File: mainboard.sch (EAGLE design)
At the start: 19 parts, among them J1 RASPBERRYPI-40-PIN-GPIO

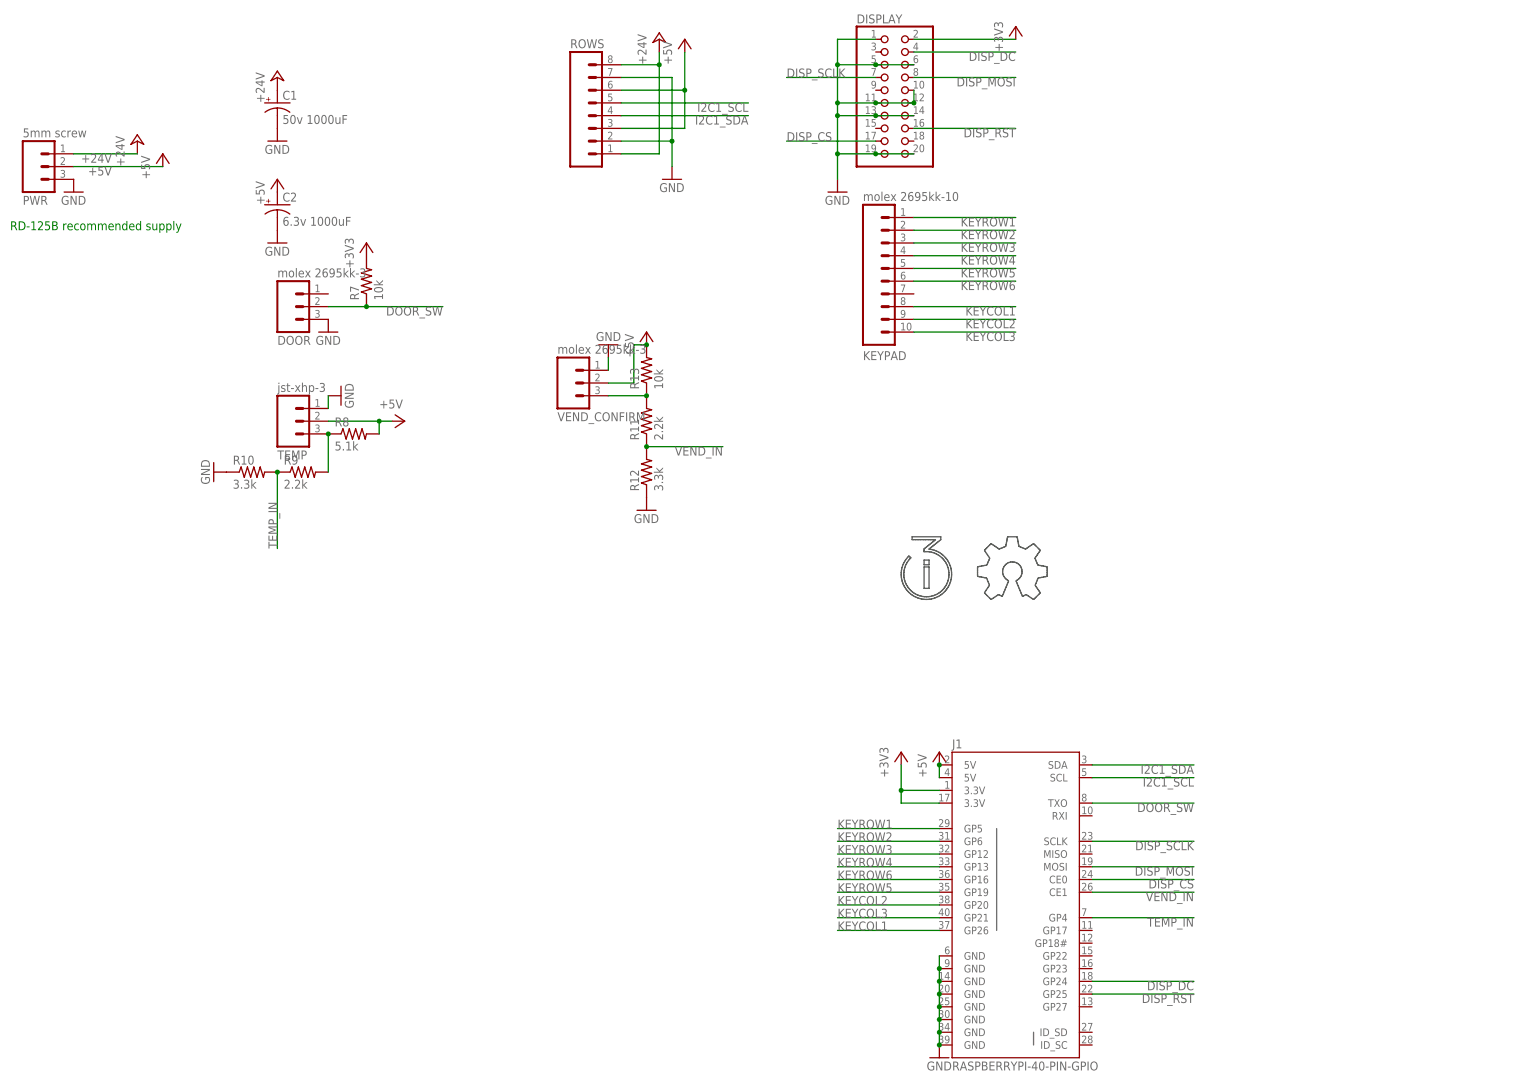
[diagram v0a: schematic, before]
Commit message: Completed mainboard design edits; buffers for keypad, reworked 5V feed.
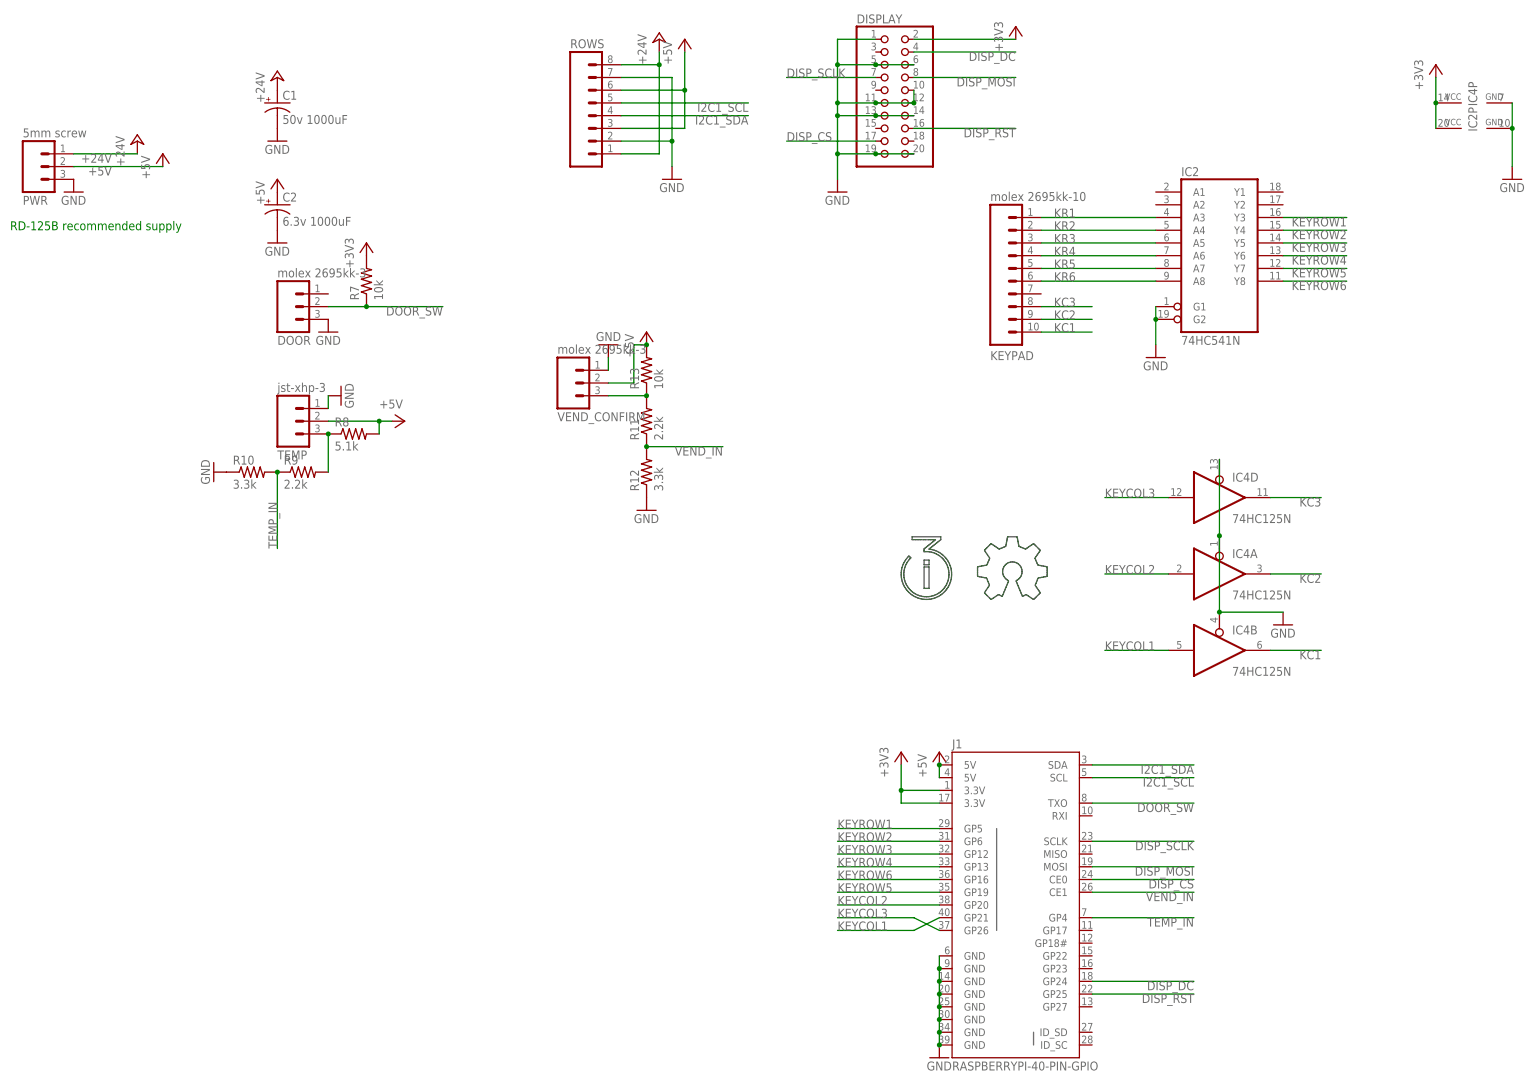
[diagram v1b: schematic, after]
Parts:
- added IC2: 74HC541N, 74xx-eu:74HC541N
- added IC4: 74HC125N, 74xx-eu:74HC125N
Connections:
- new net KC1: IC4B.O, KEYPAD.10
- new net KC2: IC4A.O, KEYPAD.9
- new net KC3: IC4D.O, KEYPAD.8
- new net KR1: IC2A.A3, KEYPAD.1
- new net KR2: IC2A.A4, KEYPAD.2
- new net KR3: IC2A.A5, KEYPAD.3
- new net KR4: IC2A.A6, KEYPAD.4
- new net KR5: IC2A.A7, KEYPAD.5
- new net KR6: IC2A.A8, KEYPAD.6
- net +3V3: now also IC2P.VCC, IC4P.VCC
- net GND: now also IC2A.G1, IC2A.G2, IC2P.GND, IC4A.OE, IC4B.OE, IC4D.OE, IC4P.GND
- net KEYCOL1: now also IC4B.I, J1.GP21; no longer J1.GP26, KEYPAD.8
- net KEYCOL2: now also IC4A.I; no longer KEYPAD.9
- net KEYCOL3: now also IC4D.I, J1.GP26; no longer J1.GP21, KEYPAD.10
- net KEYROW1: now also IC2A.Y3; no longer KEYPAD.1
- net KEYROW2: now also IC2A.Y4; no longer KEYPAD.2
- net KEYROW3: now also IC2A.Y5; no longer KEYPAD.3
- net KEYROW4: now also IC2A.Y6; no longer KEYPAD.4
- net KEYROW5: now also IC2A.Y7; no longer KEYPAD.5
- net KEYROW6: now also IC2A.Y8; no longer KEYPAD.6
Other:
- moved on the sheet: KEYPAD

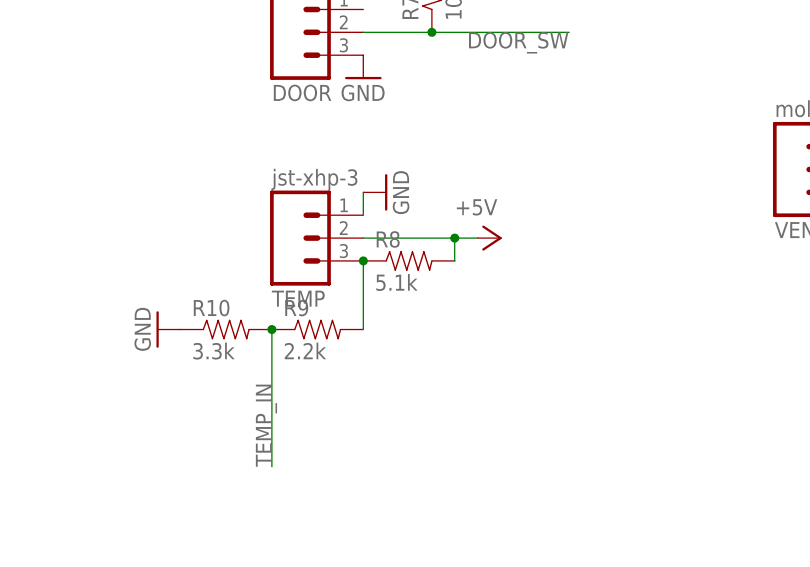
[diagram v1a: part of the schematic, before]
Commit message: No the one-wire sensor does not need a $0.252 resistor as a pull-up the $0.0254 ones are fine kthxbai.
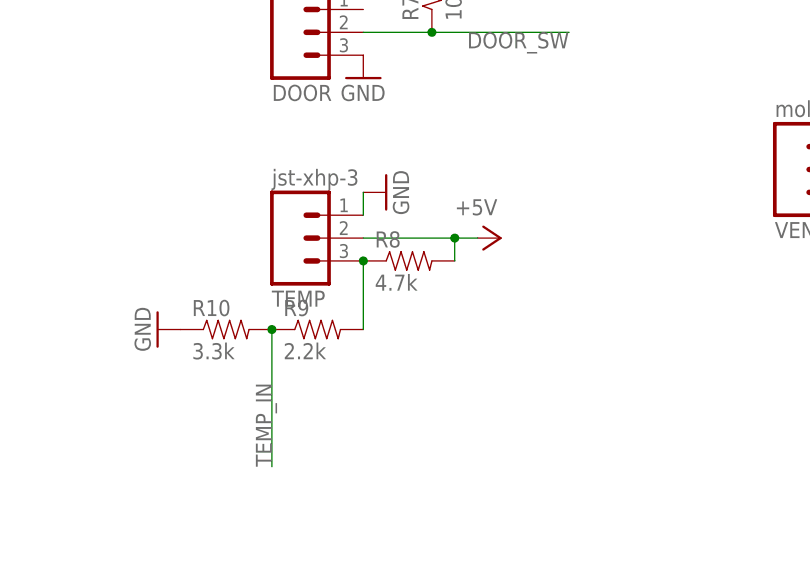
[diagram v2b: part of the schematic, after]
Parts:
- R8: value 5.1k -> 4.7k
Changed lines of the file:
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@@
 <grid distance="0.1" unitdist="inch" unit="inch" style="lines" multiple="1" display="no" altdistance="0.01" altunitdist="inch" altunit="inch"/>
 <layers>
-<layer number="1" name="Top" color="4" fill="1" visible="yes" active="no"/>
-<layer number="2" name="Route2" color="1" fill="3" visible="yes" active="no"/>
-<layer number="3" name="Route3" color="4" fill="3" visible="yes" active="no"/>
-<layer number="14" name="Route14" color="1" fill="6" visible="yes" active="no"/>
-<layer number="15" name="Route15" color="4" fill="6" visible="yes" active="no"/>
-<layer number="16" name="Bottom" color="1" fill="1" visible="yes" active="no"/>
-<layer number="17" name="Pads" color="2" fill="1" visible="yes" active="no"/>
-<layer number="18" name="Vias" color="2" fill="1" visible="yes" active="no"/>
-<layer number="19" name="Unrouted" color="6" fill="1" visible="yes" active="no"/>
-<layer number="20" name="Dimension" color="15" fill="1" visible="yes" active="no"/>
-<layer number="21" name="tPlace" color="7" fill="1" visible="yes" active="no"/>
-<layer number="22" name="bPlace" color="7" fill="1" visible="yes" active="no"/>
-<layer number="23" name="tOrigins" color="15" fill="1" visible="yes" active="no"/>
-<layer number="24" name="bOrigins" color="15" fill="1" visible="yes" active="no"/>
-<layer number="25" name="tNames" color="7" fill="1" visible="yes" active="no"/>
-<layer number="26" name="bNames" color="7" fill="1" visible="yes" active="no"/>
-<layer number="27" name="tValues" color="7" fill="1" visible="yes" active="no"/>
-<layer number="28" name="bValues" color="7" fill="1" visible="yes" active="no"/>
+<layer number="1" name="Top" color="4" fill="1" visible="no" active="no"/>
+<layer number="2" name="Route2" color="1" fill="3" visible="no" active="no"/>
+<layer number="3" name="Route3" color="4" fill="3" visible="no" active="no"/>
+<layer number="14" name="Route14" color="1" fill="6" visible="no" active="no"/>
+<layer number="15" name="Route15" color="4" fill="6" visible="no" active="no"/>
+<layer number="16" name="Bottom" color="1" fill="1" visible="no" active="no"/>
+<layer number="17" name="Pads" color="2" fill="1" visible="no" active="no"/>
+<layer number="18" name="Vias" color="2" fill="1" visible="no" active="no"/>
+<layer number="19" name="Unrouted" color="6" fill="1" visible="no" active="no"/>
+<layer number="20" name="Dimension" color="15" fill="1" visible="no" active="no"/>
+<layer number="21" name="tPlace" color="7" fill="1" visible="no" active="no"/>
+<layer number="22" name="bPlace" color="7" fill="1" visible="no" active="no"/>
+<layer number="23" name="tOrigins" color="15" fill="1" visible="no" active="no"/>
+<layer number="24" name="bOrigins" color="15" fill="1" visible="no" active="no"/>
+<layer number="25" name="tNames" color="7" fill="1" visible="no" active="no"/>
+<layer number="26" name="bNames" color="7" fill="1" visible="no" active="no"/>
+<layer number="27" name="tValues" color="7" fill="1" visible="no" active="no"/>
+<layer number="28" name="bValues" color="7" fill="1" visible="no" active="no"/>
 <layer number="29" name="tStop" color="7" fill="3" visible="no" active="no"/>
 <layer number="30" name="bStop" color="7" fill="6" visible="no" active="no"/>
@@
 <layer number="35" name="tGlue" color="7" fill="4" visible="no" active="no"/>
 <layer number="36" name="bGlue" color="7" fill="5" visible="no" active="no"/>
-<layer number="37" name="tTest" color="7" fill="1" visible="yes" active="no"/>
-<layer number="38" name="bTest" color="7" fill="1" visible="yes" active="no"/>
+<layer number="37" name="tTest" color="7" fill="1" visible="no" active="no"/>
+<layer number="38" name="bTest" color="7" fill="1" visible="no" active="no"/>
 <layer number="39" name="tKeepout" color="4" fill="11" visible="no" active="no"/>
 <layer number="40" name="bKeepout" color="1" fill="11" visible="no" active="no"/>
@@
 <layer number="44" name="Drills" color="7" fill="1" visible="no" active="no"/>
 <layer number="45" name="Holes" color="7" fill="1" visible="no" active="no"/>
-<layer number="46" name="Milling" color="3" fill="1" visible="yes" active="no"/>
-<layer number="47" name="Measures" color="7" fill="1" visible="yes" active="no"/>
-<layer number="48" name="Document" color="7" fill="1" visible="yes" active="no"/>
-<layer number="49" name="Reference" color="7" fill="1" visible="yes" active="no"/>
-<layer number="50" name="dxf" color="7" fill="1" visible="yes" active="no"/>
-<layer number="51" name="tDocu" color="7" fill="1" visible="yes" active="no"/>
-<layer number="52" name="bDocu" color="7" fill="1" visible="yes" active="no"/>
-<layer number="53" name="tGND_GNDA" color="7" fill="9" visible="yes" active="no"/>
-<layer number="54" name="bGND_GNDA" color="1" fill="9" visible="yes" active="no"/>
-<layer number="56" name="wert" color="7" fill="1" visible="yes" active="no"/>
-<layer number="57" name="tCAD" color="7" fill="1" visible="yes" active="no"/>
-<layer number="59" name="tCarbon" color="7" fill="1" visible="yes" active="no"/>
-<layer number="60" name="bCarbon" color="7" fill="1" visible="yes" active="no"/>
+<layer number="46" name="Milling" color="3" fill="1" visible="no" active="no"/>
+<layer number="47" name="Measures" color="7" fill="1" visible="no" active="no"/>
+<layer number="48" name="Document" color="7" fill="1" visible="no" active="no"/>
+<layer number="49" name="Reference" color="7" fill="1" visible="no" active="no"/>
+<layer number="50" name="dxf" color="7" fill="1" visible="no" active="no"/>
+<layer number="51" name="tDocu" color="7" fill="1" visible="no" active="no"/>
+<layer number="52" name="bDocu" color="7" fill="1" visible="no" active="no"/>
+<layer number="53" name="tGND_GNDA" color="7" fill="9" visible="no" active="no"/>
+<layer number="54" name="bGND_GNDA" color="1" fill="9" visible="no" active="no"/>
+<layer number="56" name="wert" color="7" fill="1" visible="no" active="no"/>
+<layer number="57" name="tCAD" color="7" fill="1" visible="no" active="no"/>
+<layer number="59" name="tCarbon" color="7" fill="1" visible="no" active="no"/>
+<layer number="60" name="bCarbon" color="7" fill="1" visible="no" active="no"/>
 <layer number="90" name="Modules" color="5" fill="1" visible="yes" active="yes"/>
 <layer number="91" name="Nets" color="2" fill="1" visible="yes" active="yes"/>
@@
 <part name="GND17" library="SparkFun-Aesthetics" deviceset="GND" device=""/>
 <part name="GND18" library="SparkFun-Aesthetics" deviceset="GND" device=""/>
-<part name="R8" library="SparkFun-Passives" deviceset="RESISTOR" device="1206" value="5.1k"/>
+<part name="R8" library="SparkFun-Passives" deviceset="RESISTOR" device="1206" value="4.7k"/>
 <part name="R9" library="SparkFun-Passives" deviceset="RESISTOR" device="1206" value="2.2k"/>
 <part name="R10" library="SparkFun-Passives" deviceset="RESISTOR" device="1206" value="3.3k"/>
